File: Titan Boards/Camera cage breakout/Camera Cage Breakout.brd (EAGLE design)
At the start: 101.6 x 101.6 mm, 10 parts, among them IC1 LM741D, T2 2N2222

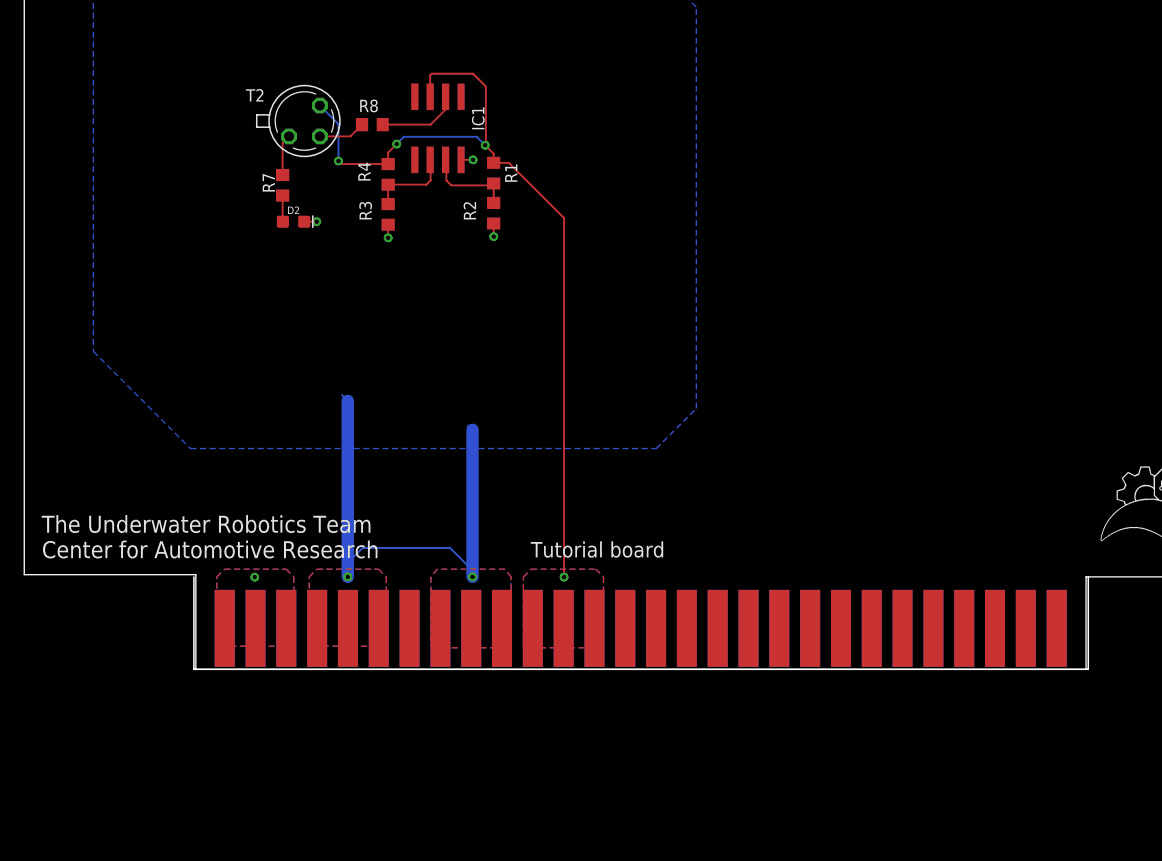
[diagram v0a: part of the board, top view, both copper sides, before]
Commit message: Library added for 8 pin molex
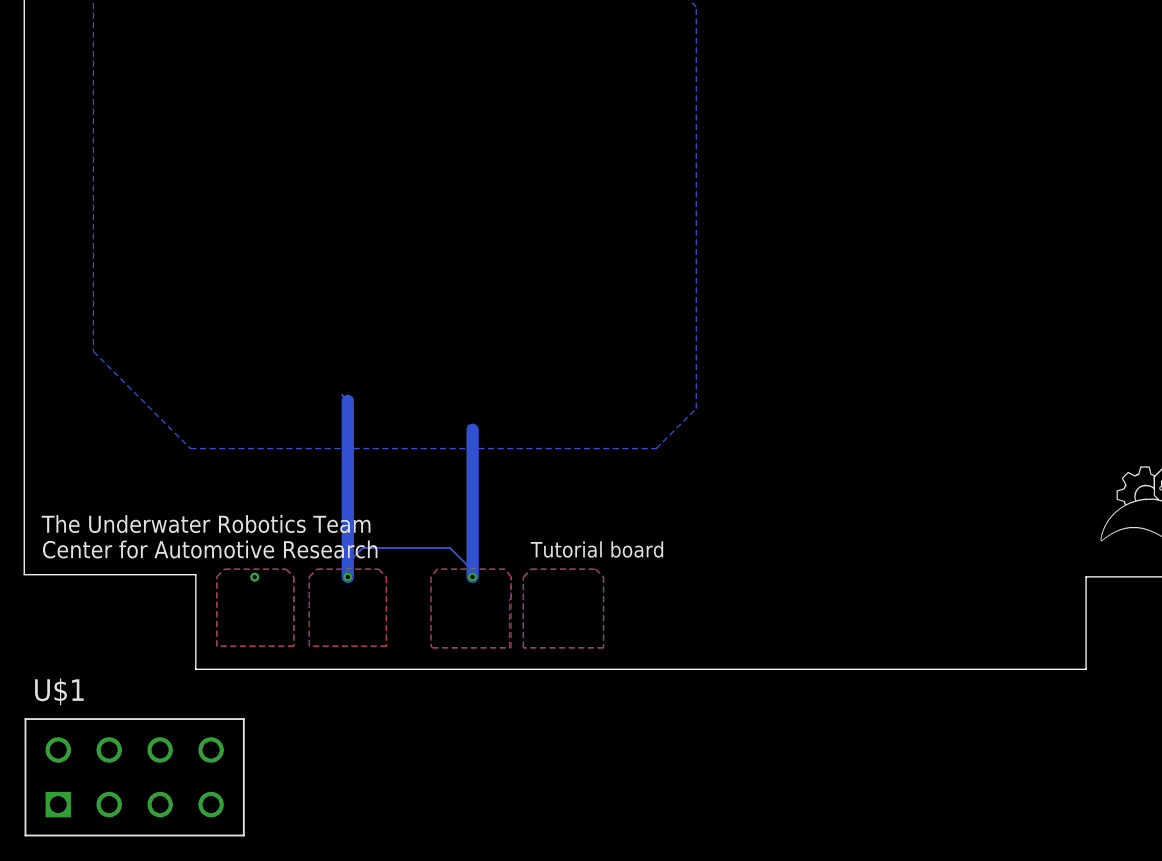
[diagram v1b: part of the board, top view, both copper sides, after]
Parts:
- removed D2: green, SparkFun-LED:LED-0603
- removed IC1: LM741D, linear:SO08
- removed R1: 2K, rcl:R0603
- removed R2, R8: 3K, rcl:R0603
- removed R3, R4: 1K, rcl:R0603
- removed R7: 560, rcl:R0603
- removed T2: 2N2222, transistor:TO18
- U$1: value 5530843-EDGE -> 8PIN_VERT; device 5530843-6:5530843-6-BOARDFINGERS -> Vertical_Connectors:8PIN_VERT
- moved U$1 11.1 mm to (9.10, -8.90)
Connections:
- removed net +3V3: U$1.1, U$1.2, U$1.3, U$1.54, U$1.55, U$1.56
- removed net +5V: IC1.7, R1.1, R4.1, T2.3, U$1.11, U$1.12, U$1.13, U$1.44, U$1.45, U$1.46
- removed net GND: D2.C, IC1.4, R2.2, R3.2, U$1.10, U$1.4, U$1.47, U$1.48, U$1.49, U$1.5, U$1.51, U$1.52, U$1.53, U$1.6, U$1.8, U$1.9
- removed net N$1: IC1.2, R3.1, R4.2
- removed net N$2: IC1.3, R1.2, R2.1
- removed net N$3: R8.1, T2.2
- removed net N$7: R7.2, T2.1
- removed net N$8: D2.A, R7.1
- removed net OUTPUT: IC1.6, R8.2
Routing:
- net +5V: track 70.0 -> 0.00 mm, vias 4 -> 0
- net N$2: track 7.39 -> 0.00 mm
- net N$1: track 6.96 -> 0.00 mm
- net OUTPUT: track 6.76 -> 0.00 mm
- net GND: track 45.2 -> 41.0 mm, vias 6 -> 2
- net N$3: track 3.88 -> 0.00 mm
- net N$7: track 3.40 -> 0.00 mm
- net N$8: track 2.16 -> 0.00 mm

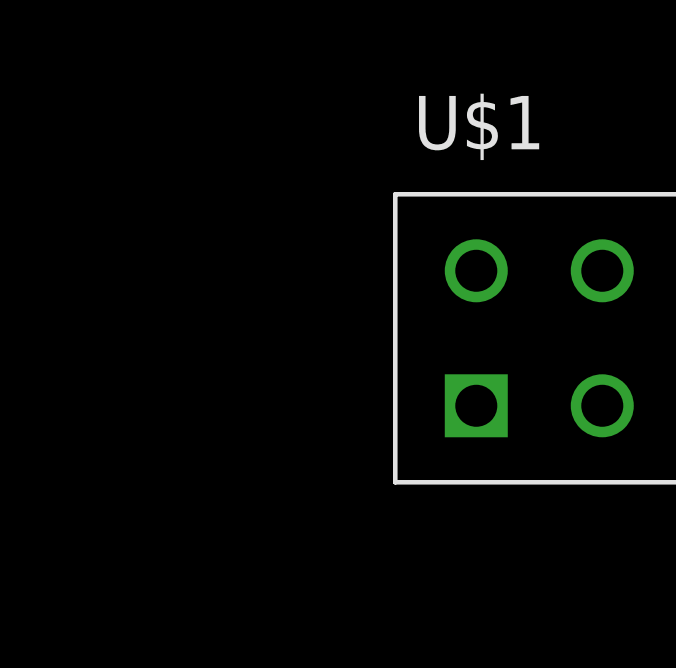
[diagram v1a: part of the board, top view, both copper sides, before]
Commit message: updated library for cage breakout
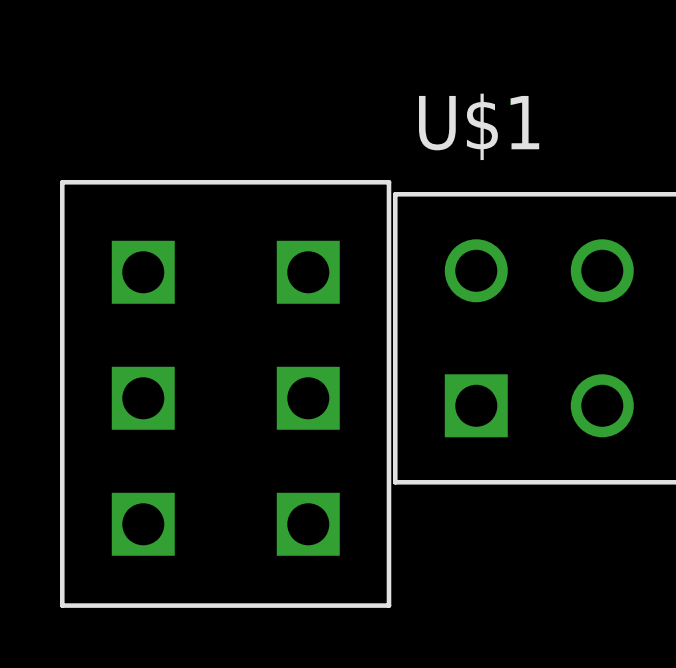
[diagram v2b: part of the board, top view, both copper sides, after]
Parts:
- added U$2: 6PIN-VERT, Vertical_Connectors:6PIN_VERT
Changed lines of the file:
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@@
 <attribute name="VALUE" x="0.7" y="-17.3" size="1.778" layer="27"/>
 </element>
+<element name="U$2" library="Vertical_Connectors" package="6PIN_VERT" value="6PIN-VERT" x="-8.3" y="-15.1" smashed="yes"/>
 </elements>
 <signals>

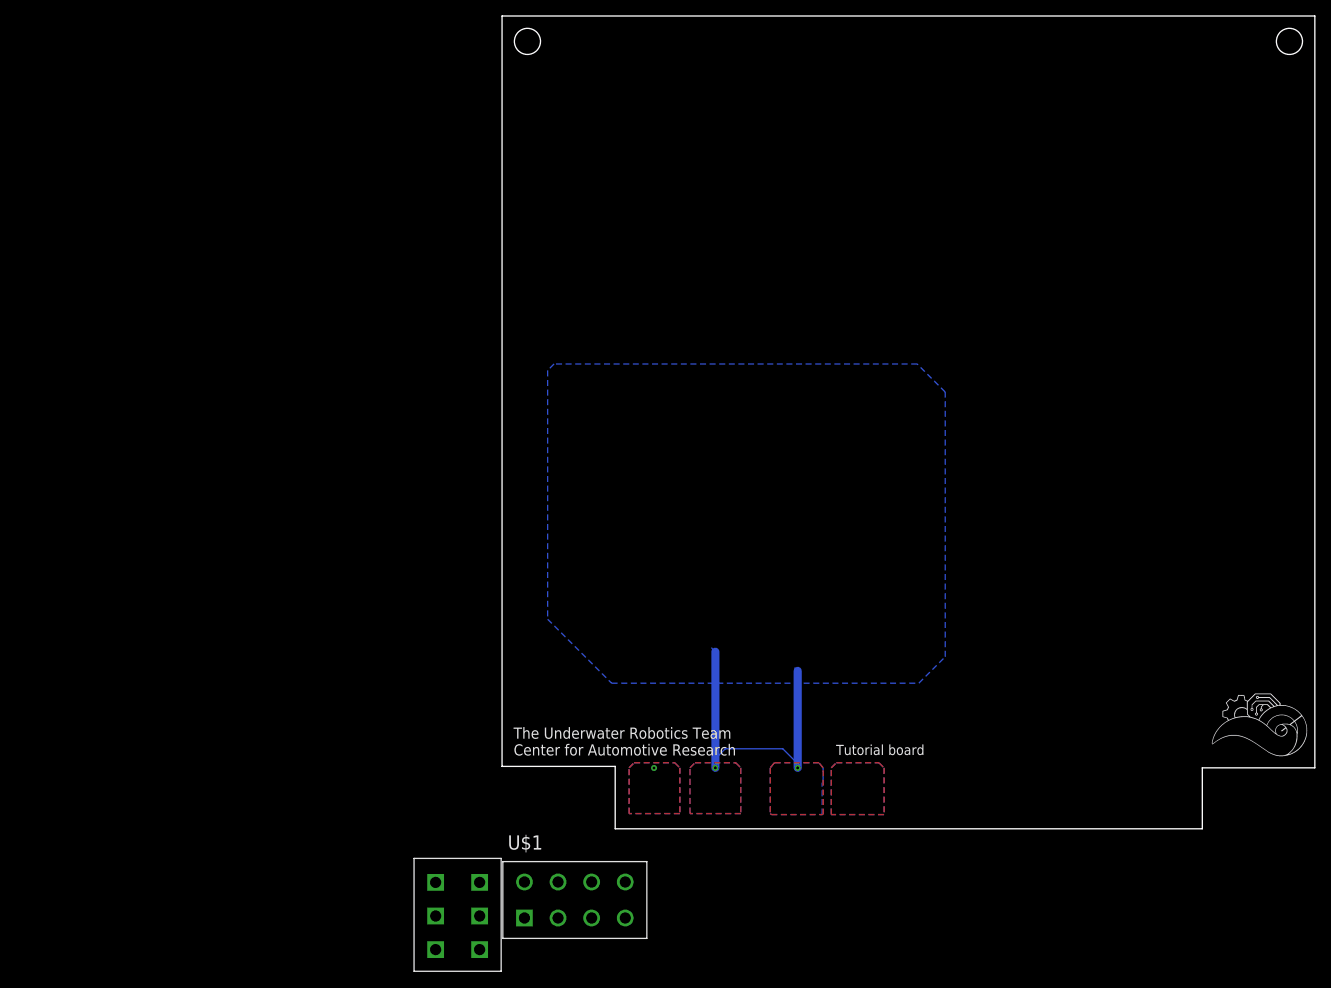
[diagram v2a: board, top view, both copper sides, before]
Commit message: schematic work for camera cage breakout
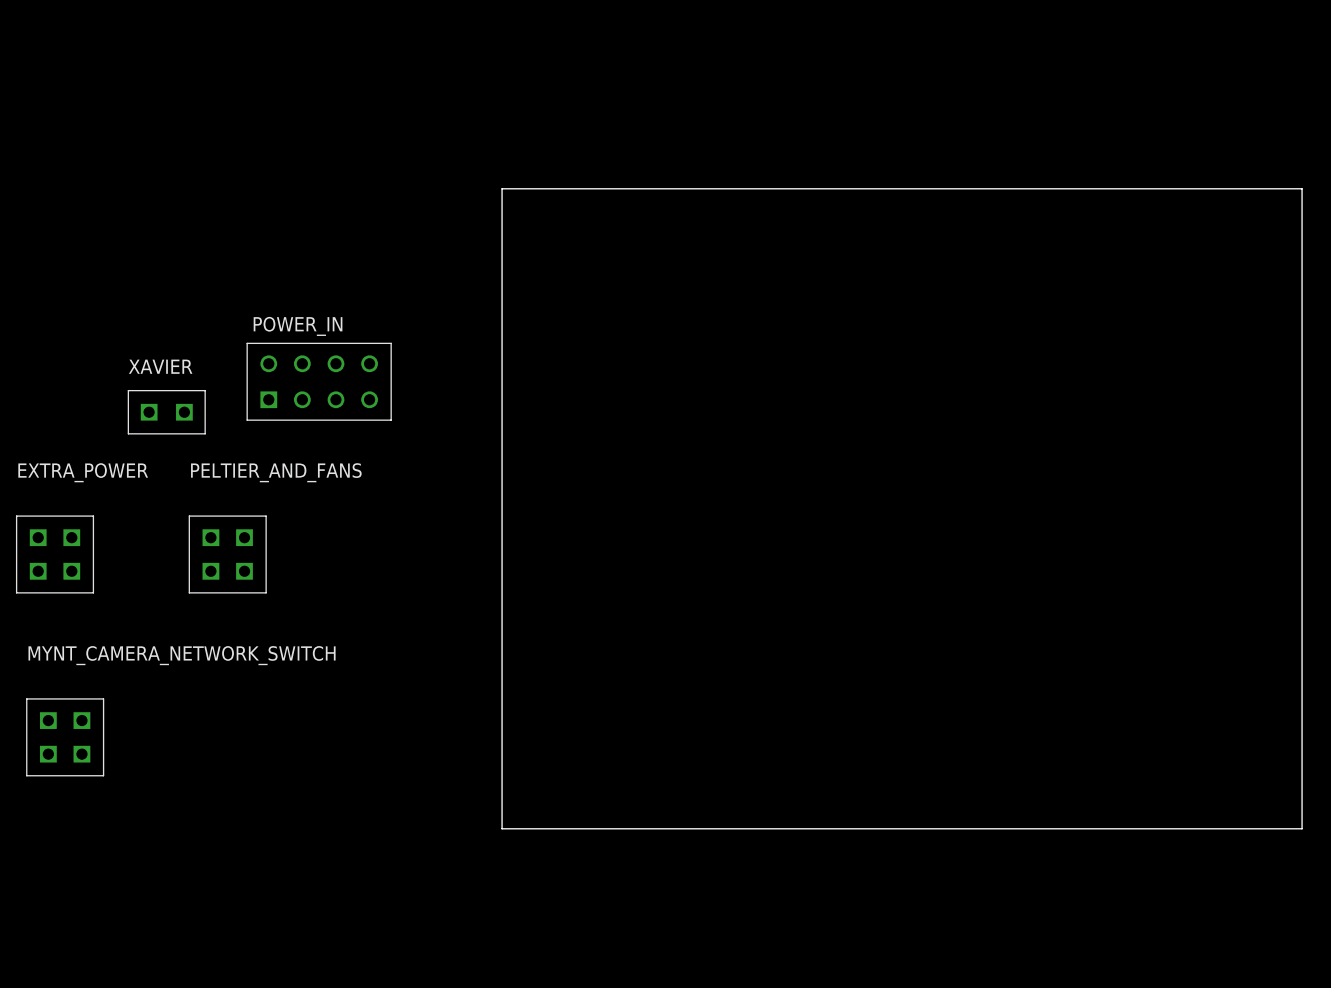
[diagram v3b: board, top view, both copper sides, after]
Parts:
- removed U$1: 8PIN_VERT, Vertical_Connectors:8PIN_VERT
- removed U$2: 6PIN-VERT, Vertical_Connectors:6PIN_VERT
- added EXTRA_POWER, MYNT_CAMERA_NETWORK_SWITCH, PELTIER_AND_FANS: 4PIN-VERT, Vertical_Connectors:4PIN-VERT
- added POWER_IN: 8PIN_VERT, Vertical_Connectors:8PIN_VERT
- added XAVIER: 2PIN-VERT, Vertical_Connectors:2PIN-VERT
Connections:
- new net 12V: EXTRA_POWER.P$1, POWER_IN.P$5
- new net 3.3V: EXTRA_POWER.P$3, POWER_IN.P$7
- new net 5V: EXTRA_POWER.P$2, MYNT_CAMERA_NETWORK_SWITCH.P$1, MYNT_CAMERA_NETWORK_SWITCH.P$2, POWER_IN.P$6
- new net GND: EXTRA_POWER.P$4, MYNT_CAMERA_NETWORK_SWITCH.P$3, MYNT_CAMERA_NETWORK_SWITCH.P$4, PELTIER_AND_FANS.P$3, PELTIER_AND_FANS.P$4, POWER_IN.P$3, POWER_IN.P$8, XAVIER.P$2
- new net N$7: POWER_IN.P$4
- new net PELTIER_SWITCHED: PELTIER_AND_FANS.P$1, PELTIER_AND_FANS.P$2, POWER_IN.P$2
- new net XAVIER_SWITCHED: POWER_IN.P$1, XAVIER.P$1
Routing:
- net GND: track 41.0 -> 0.00 mm, vias 2 -> 0
- removed copper zone on layer 1, net +3V3
- removed copper zone on layer 16, net +3V3
- removed copper zone on layer 1, net +5V
- removed copper zone on layer 16, net +5V
- removed copper zone on layer 1, net GND
- removed copper zone on layer 16, net GND
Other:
- board size 101.6 x 101.6 mm -> 100 x 80 mm
- board text removed: "The Underwater Robotics Team Center for Automotive Research"
- board text removed: "Tutorial board"
